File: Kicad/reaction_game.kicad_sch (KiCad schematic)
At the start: 7 parts, among them SW1 SW_SP86N-A1, SW2 SW_SP86N-A1, U1 RaspberryPico

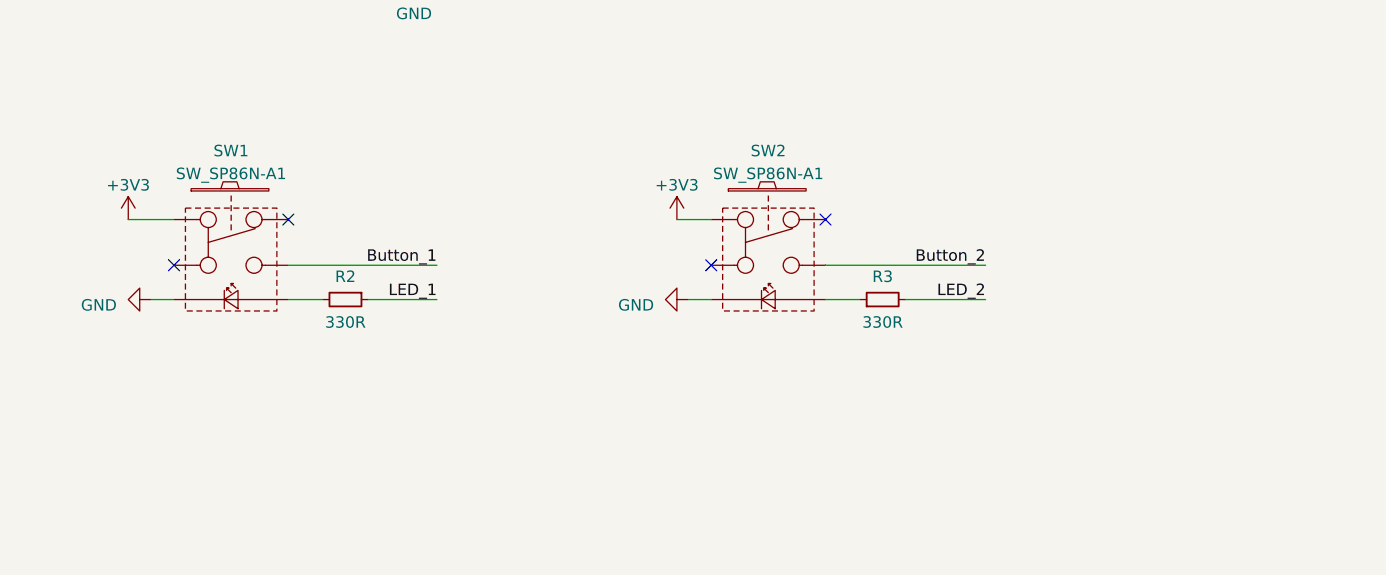
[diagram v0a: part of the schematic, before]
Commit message: PCB & initial placement
- assigned footprints
- created PCB
- initial placement of the components
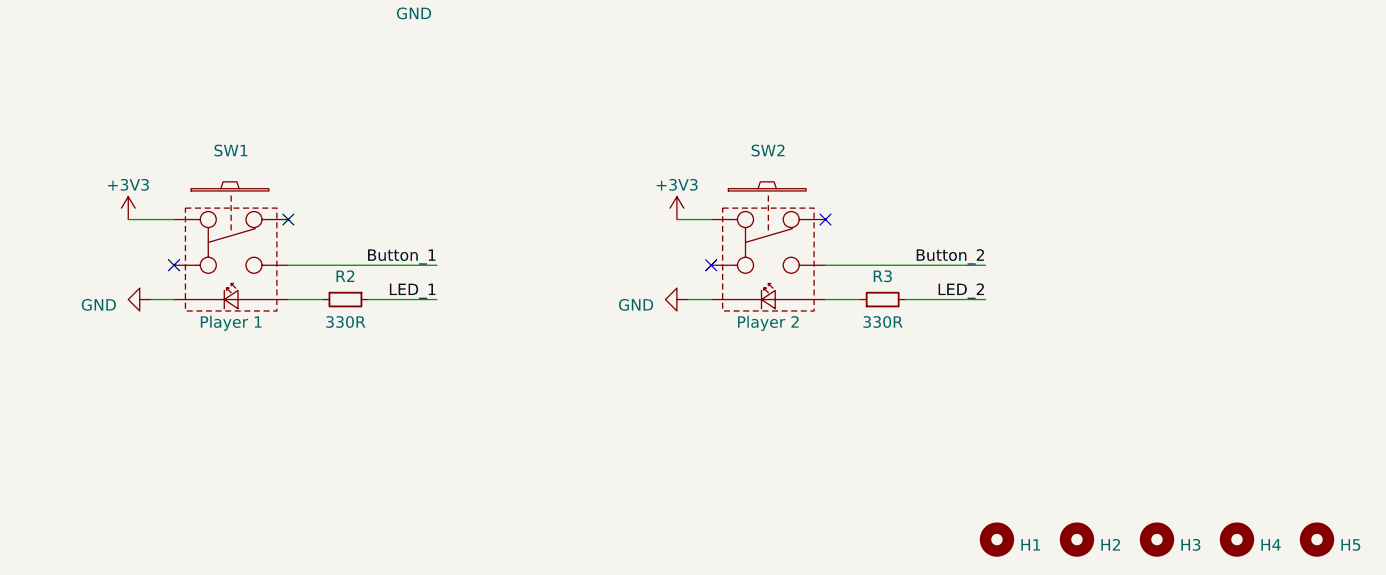
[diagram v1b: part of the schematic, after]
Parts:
- added H1, H2, H3, H4, H5: MountingHole_NPTH, MM_Various:MountingHole_3.2mm_M3_Pad_NPTH, symbol MM_Various:MountingHole_NPTH
- D1: footprint (none) -> LED_THT:LED_D8.0mm
- R1, R2, R3: footprint (none) -> MM_Various:0603C-KICAD
- SW1: value SW_SP86N-A1 -> Player 1; footprint (none) -> MM_Various:SW_PUSH-SP86N-A1-5-01
- SW2: value SW_SP86N-A1 -> Player 2; footprint (none) -> MM_Various:SW_PUSH-SP86N-A1-5-01
- U1: footprint (none) -> MM_Various:Raspberry_Pi_Pico_Rev3-THT_Offset
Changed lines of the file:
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@@
     (effects (font (size 1.27 1.27)) (justify left bottom))
   )
+  (symbol (lib_id "MM_Various:MountingHole_NPTH") (at 229.87 160.02 0) (unit 1)
+    (in_bom yes) (on_board yes) (dnp no) (fields_autoplaced)
+    (property "Reference" "H3" (at 232.41 160.655 0)
+      (effects (font (size 1.27 1.27)) (justify left))
+    )
+    (property "Value" "MountingHole_NPTH" (at 229.87 157.226 0)
+      (effects (font (size 1.27 1.27)) hide)
+    )
+    (property "Footprint" "MM_Various:MountingHole_3.2mm_M3_Pad_NPTH" (at 229.87 160.02 0)
+      (effects (font (size 1.27 1.27)) hide)
+    )
+    (property "Datasheet" "" (at 229.87 160.02 0)
+      (effects (font (size 1.27 1.27)) hide)
+    )
+    (instances
+      (project "reaction_game"
+        (path "/bdf040f4-3039-49ff-af22-f0c096c1d45c"
+          (reference "H3") (unit 1)
+        )
+      )
+    )
+  )
   (symbol (lib_id "MM_Various:LED_Small") (at 73.66 128.27 90) (unit 1)
     (in_bom yes) (on_board yes) (dnp no) (fields_autoplaced)
@@
       (effects (font (size 1.27 1.27)) (justify right))
     )
-    (property "Footprint" "" (at 73.66 128.27 90)
+    (property "Footprint" "LED_THT:LED_D8.0mm" (at 73.66 128.27 90)
       (effects (font (size 1.27 1.27)) hide)
     )
@@
       (effects (font (size 1.27 1.27)) (justify left))
     )
-    (property "Footprint" "" (at 73.66 120.65 0)
+    (property "Footprint" "MM_Various:0603C-KICAD" (at 73.66 120.65 0)
       (effects (font (size 1.27 1.27)) hide)
     )
@@
       (effects (font (size 1.27 1.27)))
     )
-    (property "Footprint" "" (at 139.7 133.35 0)
+    (property "Footprint" "MM_Various:0603C-KICAD" (at 139.7 133.35 0)
       (effects (font (size 1.27 1.27)) hide)
     )
@@
       (effects (font (size 1.524 1.524)))
     )
-    (property "Footprint" "" (at 147.32 66.04 0)
-      (effects (font (size 1.524 1.524)))
+    (property "Footprint" "MM_Various:Raspberry_Pi_Pico_Rev3-THT_Offset" (at 147.32 66.04 0)
+      (effects (font (size 1.524 1.524)) hide)
     )
     (property "Datasheet" "" (at 147.32 66.04 0)
@@
     )
   )
+  (symbol (lib_id "MM_Various:MountingHole_NPTH") (at 212.09 160.02 270) (unit 1)
+    (in_bom yes) (on_board yes) (dnp no) (fields_autoplaced)
+    (property "Reference" "H1" (at 214.63 160.655 90)
+      (effects (font (size 1.27 1.27)) (justify left))
+    )
+    (property "Value" "MountingHole_NPTH" (at 214.884 160.02 0)
+      (effects (font (size 1.27 1.27)) hide)
+    )
+    (property "Footprint" "MM_Various:MountingHole_3.2mm_M3_Pad_NPTH" (at 212.09 160.02 0)
+      (effects (font (size 1.27 1.27)) hide)
+    )
+    (property "Datasheet" "" (at 212.09 160.02 0)
+      (effects (font (size 1.27 1.27)) hide)
+    )
+    (instances
+      (project "reaction_game"
+        (path "/bdf040f4-3039-49ff-af22-f0c096c1d45c"
+          (reference "H1") (unit 1)
+        )
+      )
+    )
+  )
   (symbol (lib_id "power:GND") (at 104.14 85.09 270) (unit 1)
     (in_bom yes) (on_board yes) (dnp no) (fields_autoplaced)
@@
       (effects (font (size 1.27 1.27)))
     )
-    (property "Footprint" "" (at 199.39 133.35 0)
+    (property "Footprint" "MM_Various:0603C-KICAD" (at 199.39 133.35 0)
       (effects (font (size 1.27 1.27)) hide)
     )
@@
     )
   )
+  (symbol (lib_id "MM_Various:MountingHole_NPTH") (at 247.65 160.02 0) (unit 1)
+    (in_bom yes) (on_board yes) (dnp no) (fields_autoplaced)
+    (property "Reference" "H5" (at 250.19 160.655 0)
+      (effects (font (size 1.27 1.27)) (justify left))
+    )
+    (property "Value" "MountingHole_NPTH" (at 247.65 157.226 0)
+      (effects (font (size 1.27 1.27)) hide)
+    )
+    (property "Footprint" "MM_Various:MountingHole_3.2mm_M3_Pad_NPTH" (at 247.65 160.02 0)
+      (effects (font (size 1.27 1.27)) hide)
+    )
+    (property "Datasheet" "" (at 247.65 160.02 0)
+      (effects (font (size 1.27 1.27)) hide)
+    )
+    (instances
+      (project "reaction_game"
+        (path "/bdf040f4-3039-49ff-af22-f0c096c1d45c"
+          (reference "H5") (unit 1)
+        )
+      )
+    )
+  )
   (symbol (lib_id "power:GND") (at 147.32 96.52 0) (unit 1)
     (in_bom yes) (on_board yes) (dnp no) (fields_autoplaced)
@@
     )
   )
+  (symbol (lib_id "MM_Various:MountingHole_NPTH") (at 220.98 160.02 0) (unit 1)
+    (in_bom yes) (on_board yes) (dnp no) (fields_autoplaced)
+    (property "Reference" "H2" (at 223.52 160.655 0)
+      (effects (font (size 1.27 1.27)) (justify left))
+    )
+    (property "Value" "MountingHole_NPTH" (at 220.98 157.226 0)
+      (effects (font (size 1.27 1.27)) hide)
+    )
+    (property "Footprint" "MM_Various:MountingHole_3.2mm_M3_Pad_NPTH" (at 220.98 160.02 0)
+      (effects (font (size 1.27 1.27)) hide)
+    )
+    (property "Datasheet" "" (at 220.98 160.02 0)
+      (effects (font (size 1.27 1.27)) hide)
+    )
+    (instances
+      (project "reaction_game"
+        (path "/bdf040f4-3039-49ff-af22-f0c096c1d45c"
+          (reference "H2") (unit 1)
+        )
+      )
+    )
+  )
   (symbol (lib_id "power:+3V3") (at 115.57 124.46 0) (unit 1)
     (in_bom yes) (on_board yes) (dnp no) (fields_autoplaced)
@@
   )
   (symbol (lib_id "MM_Various:SW_SP86N-A1") (at 127 127 0) (unit 1)
-    (in_bom yes) (on_board yes) (dnp no) (fields_autoplaced)
+    (in_bom yes) (on_board yes) (dnp no)
     (property "Reference" "SW1" (at 127 116.84 0)
       (effects (font (size 1.27 1.27)))
     )
-    (property "Value" "SW_SP86N-A1" (at 127 119.38 0)
-      (effects (font (size 1.27 1.27)))
-    )
-    (property "Footprint" "" (at 127 127 0)
-      (effects (font (size 1.524 1.524)))
+    (property "Value" "Player 1" (at 127 135.89 0)
+      (effects (font (size 1.27 1.27)))
+    )
+    (property "Footprint" "MM_Various:SW_PUSH-SP86N-A1-5-01" (at 127 127 0)
+      (effects (font (size 1.524 1.524)) hide)
     )
     (property "Datasheet" "" (at 127 127 0)
@@
   )
   (symbol (lib_id "MM_Various:SW_SP86N-A1") (at 186.69 127 0) (unit 1)
-    (in_bom yes) (on_board yes) (dnp no) (fields_autoplaced)
+    (in_bom yes) (on_board yes) (dnp no)
     (property "Reference" "SW2" (at 186.69 116.84 0)
       (effects (font (size 1.27 1.27)))
     )
-    (property "Value" "SW_SP86N-A1" (at 186.69 119.38 0)
-      (effects (font (size 1.27 1.27)))
-    )
-    (property "Footprint" "" (at 186.69 127 0)
-      (effects (font (size 1.524 1.524)))
+    (property "Value" "Player 2" (at 186.69 135.89 0)
+      (effects (font (size 1.27 1.27)))
+    )
+    (property "Footprint" "MM_Various:SW_PUSH-SP86N-A1-5-01" (at 186.69 127 0)
+      (effects (font (size 1.524 1.524)) hide)
     )
     (property "Datasheet" "" (at 186.69 127 0)
@@
         )
       )
+    )
+  )
+  (symbol (lib_id "MM_Various:MountingHole_NPTH") (at 238.76 160.02 0) (unit 1)
+    (in_bom yes) (on_board yes) (dnp no) (fields_autoplaced)
+    (property "Reference" "H4" (at 241.3 160.655 0)
+      (effects (font (size 1.27 1.27)) (justify left))
+    )
+    (property "Value" "MountingHole_NPTH" (at 238.76 157.226 0)
+      (effects (font (size 1.27 1.27)) hide)
+    )
+    (property "Footprint" "MM_Various:MountingHole_3.2mm_M3_Pad_NPTH" (at 238.76 160.02 0)
+      (effects (font (size 1.27 1.27)) hide)
+    )
+    (property "Datasheet" "" (at 238.76 160.02 0)
+      (effects (font (size 1.27 1.27)) hide)
+    )
+    (instances
+      (project "reaction_game"
+        (path "/bdf040f4-3039-49ff-af22-f0c096c1d45c"
+          (reference "H4") (unit 1)
+        )
+      )

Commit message: 3D models, placement
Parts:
- removed H5: MountingHole_NPTH, MM_Various:MountingHole_3.2mm_M3_Pad_NPTH, symbol MM_Various:MountingHole_NPTH
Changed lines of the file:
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@@
-    )
-  )
-  (symbol (lib_id "MM_Various:MountingHole_NPTH") (at 247.65 160.02 0) (unit 1)
-    (in_bom yes) (on_board yes) (dnp no) (fields_autoplaced)
-    (property "Reference" "H5" (at 250.19 160.655 0)
-      (effects (font (size 1.27 1.27)) (justify left))
-    )
-    (property "Value" "MountingHole_NPTH" (at 247.65 157.226 0)
-      (effects (font (size 1.27 1.27)) hide)
-    )
-    (property "Footprint" "MM_Various:MountingHole_3.2mm_M3_Pad_NPTH" (at 247.65 160.02 0)
-      (effects (font (size 1.27 1.27)) hide)
-    )
-    (property "Datasheet" "" (at 247.65 160.02 0)
-      (effects (font (size 1.27 1.27)) hide)
-    )
-    (instances
-      (project "reaction_game"
-        (path "/bdf040f4-3039-49ff-af22-f0c096c1d45c"
-          (reference "H5") (unit 1)
-        )
-      )
     )
   )

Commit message: Finished routing
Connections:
- net Button_1: now also U1.2 (GP1/SPI0_CSn/I2C0_SCL/UART0_RX); no longer U1.1 (GP0/SPI0_RX/I2C0_SDA/UART0_TX)
- net LED_1: now also U1.1 (GP0/SPI0_RX/I2C0_SDA/UART0_TX); no longer U1.2 (GP1/SPI0_CSn/I2C0_SCL/UART0_RX)
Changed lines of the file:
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@@
     (stroke (width 0) (type default))
-  )
-  (label "Button_1" (at 86.36 41.91 0) (fields_autoplaced)
-    (effects (font (size 1.27 1.27)) (justify left bottom))
   )
   (label "LED_2" (at 210.82 133.35 180) (fields_autoplaced)
@@
     (effects (font (size 1.27 1.27)) (justify right bottom))
   )
-  (label "LED_1" (at 86.36 44.45 0) (fields_autoplaced)
+  (label "Game_LED" (at 85.09 57.15 0) (fields_autoplaced)
     (effects (font (size 1.27 1.27)) (justify left bottom))
   )
-  (label "Game_LED" (at 85.09 57.15 0) (fields_autoplaced)
+  (label "Button_1" (at 86.36 44.45 0) (fields_autoplaced)
     (effects (font (size 1.27 1.27)) (justify left bottom))
   )
@@
     (effects (font (size 1.27 1.27)) (justify left bottom))
   )
+  (label "LED_1" (at 86.36 41.91 0) (fields_autoplaced)
+    (effects (font (size 1.27 1.27)) (justify left bottom))
+  )
